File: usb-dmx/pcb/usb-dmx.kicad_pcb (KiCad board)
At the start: 2 copper layers, 25 x 35 mm, 21 parts, among them J1 USB_C_Receptacle_USB2.0_16P, J2 USB_A, SW1 PTS526_SM15_SMTR2_LFS, U1 IP4234CZ6, U2 ADP2108AUJ-3.3, U3 ESP32-S3-MINI-1U, U4 ST485E

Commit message: updating gerber files
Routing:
- net 15: track 22.0 -> 0.00 mm
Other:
- board text added: "TRANCE USB-DMX Rev: 1.1"
- board text removed: "TRANCE USB-DMX Rev: 1"
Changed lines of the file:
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@@
 			(psa4output no)
 			(plot_black_and_white yes)
-			(plotinvisibletext no)
 			(sketchpadsonfab no)
 			(plotpadnumbers no)
@@
 		)
 	)
-	(gr_text "TRANCE\nUSB-DMX\nRev: 1"
+	(gr_text "TRANCE\nUSB-DMX\nRev: 1.1"
 		(at 100 74 0)
 		(layer "B.SilkS")
@@
 		(layer "Cmts.User")
 		(pts
-			(xy 109.9 62) (xy 111.1 62)
+			(xy 109.6 62) (xy 111.4 62)
 		)
 		(height -5.5)
@@
 			(keep_text_aligned yes)
 		)
-		(gr_text "1.2"
+		(gr_text "1.8"
 			(at 110.5 55.35 0)
 			(layer "Cmts.User")
@@
 	)
 	(segment
-		(start 109.2 70.6)
-		(end 109.2 76.8)
-		(width 0.2)
-		(layer "F.Cu")
-		(net 8)
-	)
-	(segment
-		(start 103.997 74.551)
-		(end 106.449 74.551)
-		(width 0.2)
-		(layer "F.Cu")
-		(net 8)
-	)
-	(segment
-		(start 107.4 73.6)
-		(end 107.4 70.6)
-		(width 0.2)
-		(layer "F.Cu")
-		(net 8)
-	)
-	(segment
-		(start 107.4 70.6)
-		(end 107.8 70.2)
-		(width 0.2)
-		(layer "F.Cu")
-		(net 8)
-	)
-	(segment
-		(start 108.8 70.2)
-		(end 109.2 70.6)
-		(width 0.2)
-		(layer "F.Cu")
-		(net 8)
-	)
-	(segment
-		(start 99.4 79.148)
-		(end 103.997 74.551)
-		(width 0.2)
-		(layer "F.Cu")
-		(net 8)
-	)
-	(segment
-		(start 106.449 74.551)
-		(end 107.4 73.6)
-		(width 0.2)
-		(layer "F.Cu")
-		(net 8)
-	)
-	(segment
-		(start 107.8 70.2)
-		(end 108.8 70.2)
-		(width 0.2)
-		(layer "F.Cu")
-		(net 8)
-	)
-	(segment
-		(start 99.4 79.5)
-		(end 99.4 79.148)
-		(width 0.2)
-		(layer "F.Cu")
-		(net 8)
-	)
-	(segment
 		(start 100.4 76.6875)
 		(end 100.4125 76.7)
@@
 	)
 	(segment
+		(start 103.352 89.9)
+		(end 104 89.252)
+		(width 0.2)
+		(layer "F.Cu")
+		(net 15)
+	)
+	(segment
 		(start 107.7125 81.8)
 		(end 109.3375 81.8)
@@
 	)
 	(segment
-		(start 103.701 89.551)
-		(end 103.701 81.599)
+		(start 104 89.252)
+		(end 104 81.3)
 		(width 0.2)
 		(layer "F.Cu")
@@
 	)
 	(segment
-		(start 103.352 89.9)
-		(end 103.701 89.551)
+		(start 104 81.3)
+		(end 105.2 80.1)
 		(width 0.2)
 		(layer "F.Cu")
@@
 	)
 	(segment
-		(start 103.701 81.599)
-		(end 105.2 80.1)
-		(width 0.2)
-		(layer "F.Cu")
-		(net 15)
-	)
-	(segment
 		(start 109.5 81.8)
 		(end 111.2 80.1)
@@
 	)
 	(via
-		(at 104.9 86.9)
+		(at 105 86)
 		(size 0.6)
 		(drill 0.3)

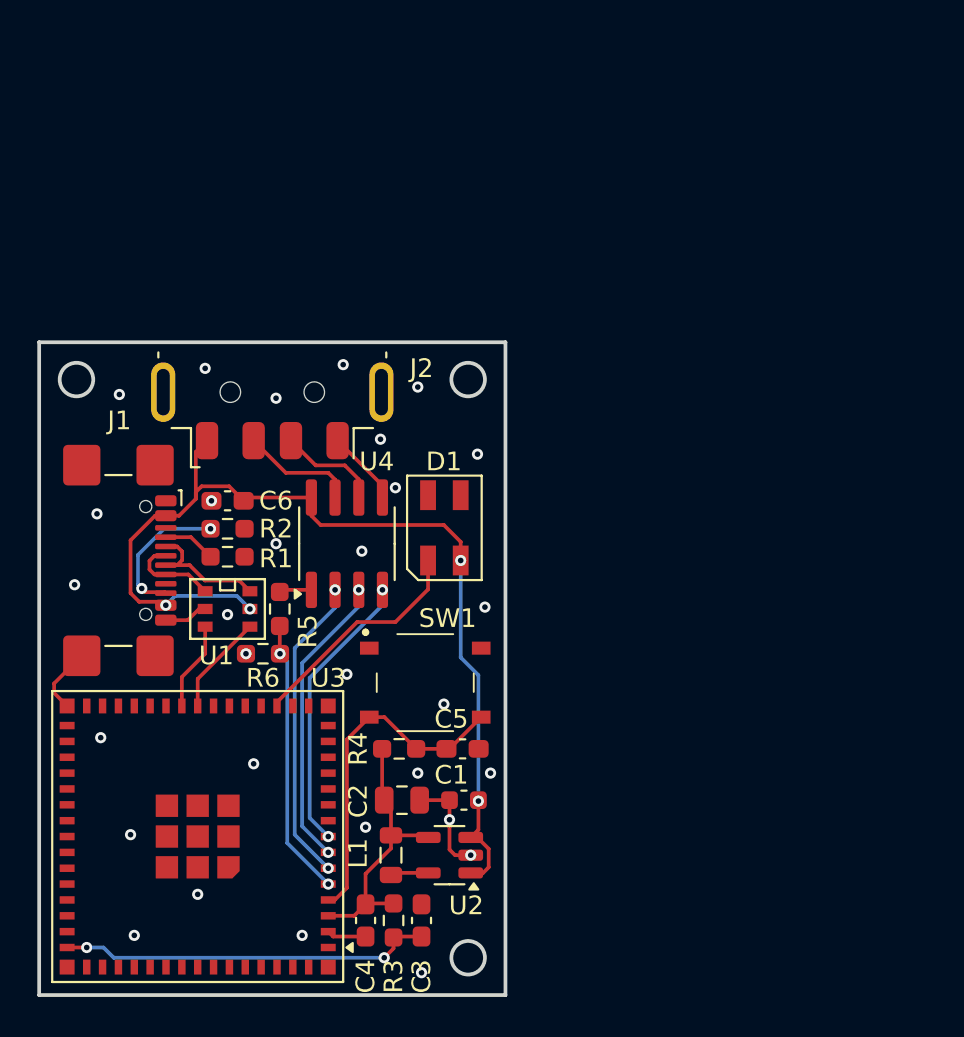
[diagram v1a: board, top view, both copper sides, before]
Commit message: adding larger capacitor to esp and exchanging parts
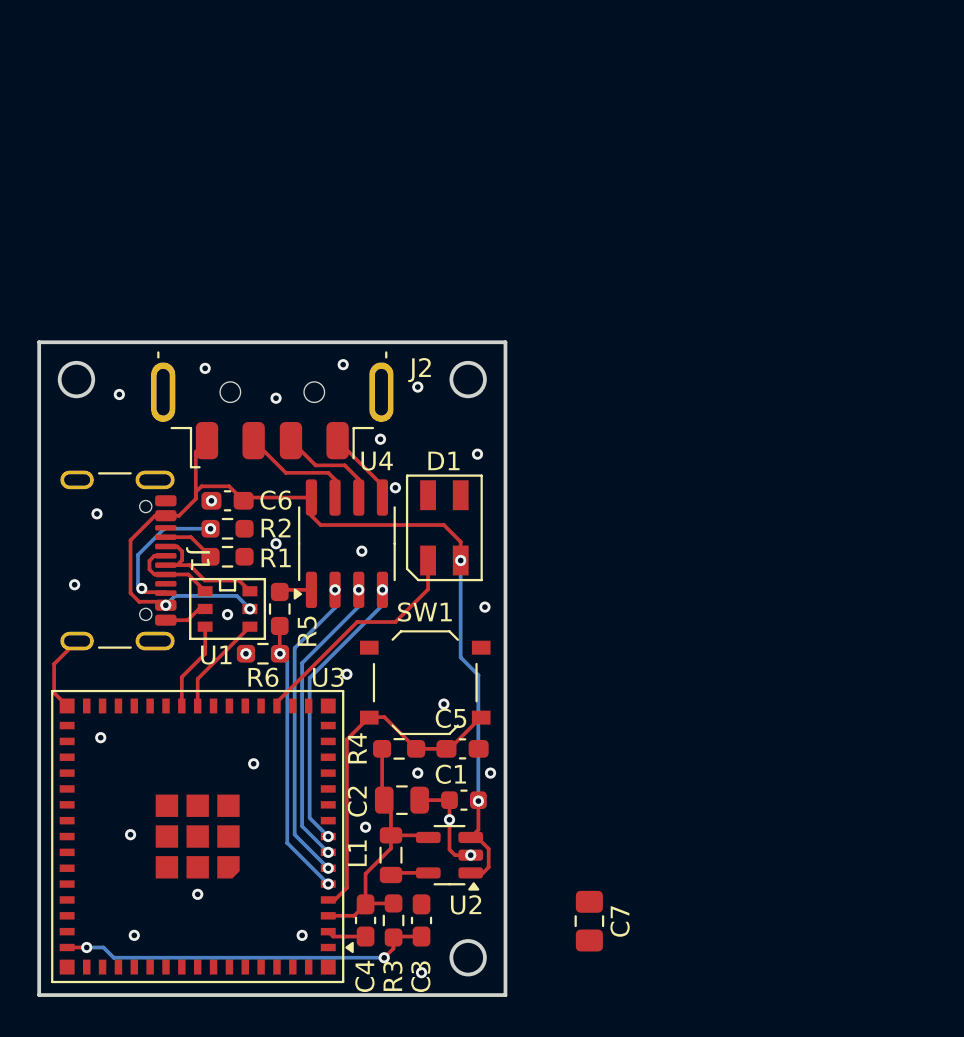
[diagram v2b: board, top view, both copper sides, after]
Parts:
- added C7: 47uF, Capacitor_SMD:C_0805_2012Metric_Pad1.18x1.45mm_HandSolder, F.Cu at (117.0, 91.0)
- J1: footprint Connector_USB:USB_C_Receptacle_GCT_USB4110 -> Connector_USB:USB_C_Receptacle_GCT_USB4105-xx-A_16P_TopMnt_Horizontal
- SW1: footprint footprints:PTS526SM15SMTR2LFS -> Button_Switch_SMD:SW_Push_1P1T_XKB_TS-1187A
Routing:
- net GND: track 17.6 -> 18.3 mm

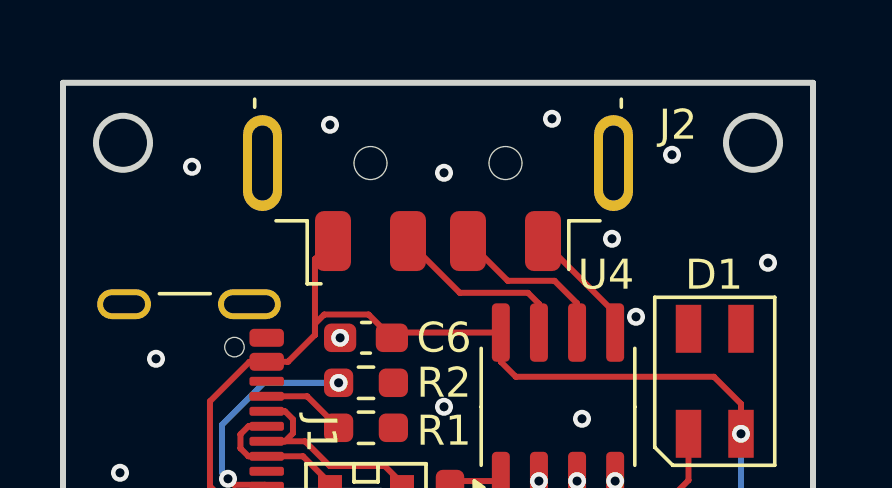
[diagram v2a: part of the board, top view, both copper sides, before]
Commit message: fingind aliexpress alternatives
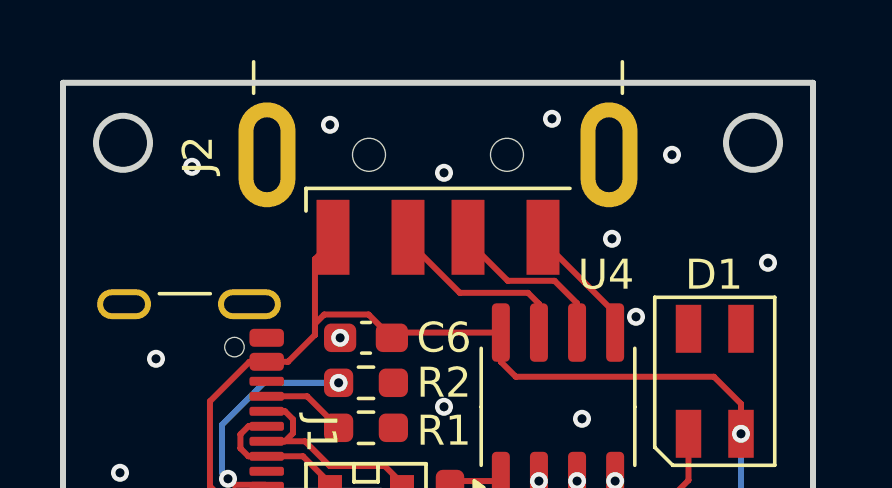
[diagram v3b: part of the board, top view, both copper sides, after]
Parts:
- J2: footprint Connector_USB:USB_A_Molex_48037-2200_Horizontal -> Connector_USB:USB_A_CNCTech_1001-011-01101_Horizontal
- moved J2 1.20 mm to (100.0, 55.5)

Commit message: creating pcb layout
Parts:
- removed L1: 1uH, Inductor_SMD:L_0805_2012Metric
- removed SW1: PTS526_SM15_SMTR2_LFS, Button_Switch_SMD:SW_Push_1P1T_XKB_TS-1187A
- removed U2: ADP2108AUJ-3.3, Package_TO_SOT_SMD:TSOT-23-5
- added SW2: SW_Push, Button_Switch_SMD:SW_Push_1P1T_XKB_TS-1187A, F.Cu at (94.1, 68.8)
- added U5: MAX485E, Package_SO:SOP-8_3.76x4.96mm_P1.27mm, F.Cu at (106.8, 55.5)
- C1: value 4.7uF -> 22uF; footprint Capacitor_SMD:C_0603_1608Metric -> Capacitor_SMD:C_0805_2012Metric
- C2: value 10uF -> 22uF
- C5: footprint Capacitor_SMD:C_0603_1608Metric_Pad1.08x0.95mm_HandSolder -> Capacitor_SMD:C_0603_1608Metric
- R4: footprint Resistor_SMD:R_0603_1608Metric_Pad0.98x0.95mm_HandSolder -> Resistor_SMD:R_0603_1608Metric
- U1: value IP4234CZ6 -> AMS1117-3.3; footprint footprints:IP4234CZ6_SOT-457-6 -> Package_TO_SOT_SMD:SOT-223-3_TabPin2
- U4: value ST485E -> USBLC6-2SC6; footprint Package_SO:SOIC-8_3.9x4.9mm_P1.27mm -> Package_TO_SOT_SMD:SOT-23-6
- moved C5 24.8 mm to (91.8, 65.2), turned to 180 degrees
- moved R6 20.7 mm to (100.2, 56.0), turned to 0 degrees
- moved R4 20.5 mm to (94.8, 65.2), turned to 180 degrees
- moved C2 17.6 mm to (99.2, 68.8), turned to 90 degrees
- moved R1 17.2 mm to (100.2, 54.5)
- moved R5 16.8 mm to (100.2, 57.5), turned to 0 degrees
- moved C6 15.7 mm to (100.2, 53.0), turned to 0 degrees
- moved J2 15.5 mm to (100.0, 40.0)
- moved J1 15.2 mm to (93.6, 56.8)
- moved C3 14.9 mm to (106.8, 76.2)
- moved C1 11.9 mm to (107.8, 72.9)
- moved C7 11.4 mm to (107.0, 85.5)
- moved R3 11.4 mm to (106.8, 79.7), turned to 90 degrees
- moved R2 11.3 mm to (100.2, 59.0)
- moved U1 9.51 mm to (104.8, 68.2)
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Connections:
- C1 pad 1: VCC_5V -> VCC_3.3V
- C2 pad 1: VCC_3.3V -> VCC_5V
- R5 pad 2: Net-(U4-RO) -> Net-(U5-RO)
- U1 pad 1: Net-(J1-D+-PadA6) -> GND
- U1 pad 2: GND -> VCC_3.3V
- U1 pad 3: D+ -> VCC_5V
- U4 pad 1: Net-(U4-RO) -> Net-(J1-D+-PadA6)
- U4 pad 2: 2 -> GND
- U4 pad 3: 3 -> Net-(J1-D--PadA7)
- U4 pad 4: 4 -> D-
- U4 pad 5: GND -> VCC_5V
- U4 pad 6: DMX+ -> D+
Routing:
- net GND: track 18.3 -> 45.0 mm, vias 30 -> 33
- net VCC_3.3V: track 14.9 -> 38.7 mm
- net 0: track 18.3 -> 40.3 mm, vias 0 -> 2
- net VCC_5V: track 54.2 -> 70.6 mm, vias 4 -> 2
- net 1: track 14.9 -> 29.6 mm
- net D+: track 4.77 -> 13.7 mm, vias 0 -> 2
- net 2: track 16.6 -> 24.9 mm
- net 3: track 15.9 -> 24.0 mm
- net 4: track 15.3 -> 23.2 mm
- net Net-(J1-D+-PadA6): track 4.92 -> 10.4 mm
- net D-: track 5.41 -> 10.0 mm, vias 0 -> 2
- net Net-(U5-RO): track 0.00 -> 3.80 mm
- net Net-(U3-EN): track 20.0 -> 23.5 mm
- net DMX-: track 6.19 -> 9.48 mm
- net DMX+: track 5.47 -> 8.34 mm
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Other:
- board size 25 x 35 mm -> 20 x 44 mm
- board text added: "${REFERENCE}"
- board text added: "TRANCE USB-DMX Rev: 1.2"
- board text removed: "TRANCE USB-DMX Rev: 1.1"

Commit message: updating documentation
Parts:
- moved C4 36.3 mm to (133.0, 58.8), turned to 0 degrees
- moved C7 35.9 mm to (132.8, 60.5), turned to 0 degrees
- moved U3 30.8 mm to (127.0, 69.5), turned to -90 degrees
- moved J2 30.3 mm to (87.2, 67.5), turned to 180 degrees
- moved R3 27.6 mm to (126.9, 60.6), turned to 180 degrees
- moved C5 23.3 mm to (112.5, 75.8), turned to -90 degrees
- moved C3 22.7 mm to (123.4, 60.6), turned to 180 degrees
- moved SW2 22.4 mm to (116.0, 73.4), turned to 90 degrees
- moved J1 20.1 mm to (104.1, 73.9), turned to 0 degrees
- moved R4 19.3 mm to (112.5, 72.8), turned to -90 degrees
- moved C1 18.1 mm to (120.2, 59.7), turned to -90 degrees
- moved C2 16.8 mm to (116.0, 68.2), turned to 180 degrees
- moved C6 14.2 mm to (100.2, 67.2), turned to 90 degrees
- moved R1 12.8 mm to (101.8, 67.2), turned to 90 degrees
- moved U1 11.9 mm to (115.4, 62.6), turned to 90 degrees
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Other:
- board size 20 x 44 mm -> 44 x 20 mm

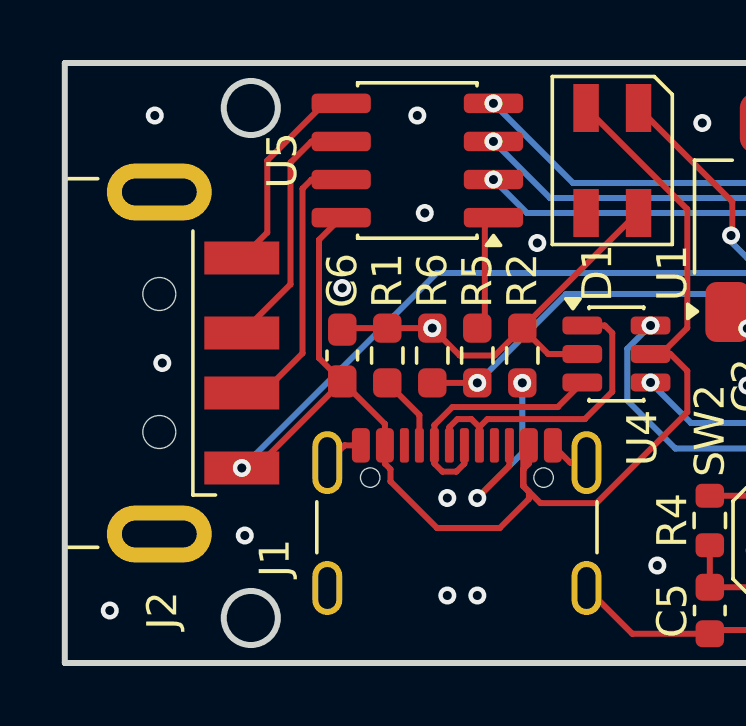
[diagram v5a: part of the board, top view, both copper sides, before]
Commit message: moving usb-a-plug, changing esp32-partnumber
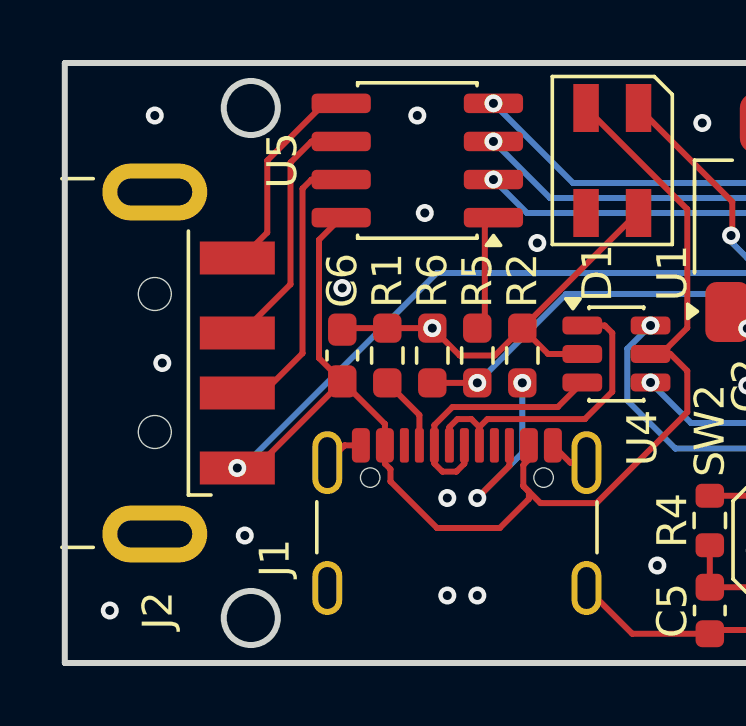
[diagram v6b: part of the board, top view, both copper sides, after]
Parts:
- moved J2 0.15 mm to (87.1, 67.5)
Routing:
- net VCC_5V: track 70.6 -> 69.4 mm
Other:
- board text added: "TRANCE USB-DMX Rev: 1.3"
- board text removed: "TRANCE USB-DMX Rev: 1.2"
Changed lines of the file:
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@@
 		(title "TRANCE USB-DMX")
 		(date "2025-12-23")
-		(rev "1.2")
+		(rev "1.3")
 		(company "Hafen Innovation")
 		(comment 1 "Author: Samuel Hafen")
@@
 			(drillshape 0)
 			(scaleselection 1)
-			(outputdirectory "gbr/")
+			(outputdirectory "gerber/")
 		)
 	)
@@
 	(footprint "Connector_USB:USB_A_CNCTech_1001-011-01101_Horizontal"
 		(layer "F.Cu")
-		(at 87.25 67.5 180)
+		(at 87.1 67.5 180)
 		(descr "USB type A Plug, Horizontal, http://cnctech.us/pdfs/1001-011-01101.pdf")
 		(tags "USB-A")
@@
 		)
 	)
-	(gr_text "TRANCE\nUSB-DMX\nRev: 1.2"
+	(gr_text "TRANCE\nUSB-DMX\nRev: 1.3"
 		(at 120 67.5 90)
 		(layer "B.SilkS")
@@
 	)
 	(segment
-		(start 106.47 70.245)
-		(end 106.284 70.431)
-		(width 0.2)
-		(layer "F.Cu")
-		(net 24)
-	)
-	(segment
 		(start 101.67 70.245)
 		(end 101.67 69.5325)
@@
 	)
 	(segment
-		(start 97.3625 71)
-		(end 100.25 68.1125)
+		(start 106.47 70.245)
+		(end 106.47 70.714)
 		(width 0.2)
 		(layer "F.Cu")
@@
 	)
 	(segment
-		(start 111.75 62.375)
-		(end 108.375 59)
+		(start 96.75 71)
+		(end 97.3625 71)
 		(width 0.2)
 		(layer "F.Cu")
@@
 	)
 	(segment
-		(start 96.9 71)
-		(end 97.3625 71)
+		(start 111.75 62.375)
+		(end 108.375 59)
 		(width 0.2)
 		(layer "F.Cu")
@@
 	)
 	(segment
-		(start 106.47 70.853992)
-		(end 106.284 71.039992)
+		(start 97.3625 71)
+		(end 100.25 68.1125)
 		(width 0.2)
 		(layer "F.Cu")
@@
 	)
 	(segment
-		(start 106.284 70.431)
+		(start 106.47 70.714)
+		(end 106.284 70.9)
+		(width 0.2)
+		(layer "F.Cu")
+		(net 24)
+	)
+	(segment
+		(start 106.284 70.9)
 		(end 106.284 71.600008)
 		(width 0.2)
@@
 	)
 	(segment
-		(start 106.47 70.245)
-		(end 106.47 70.853992)
-		(width 0.2)
-		(layer "F.Cu")
-		(net 24)
-	)
-	(segment
 		(start 116.95 68.25)
 		(end 116.95 66.55)
@@
 	)
 	(segment
-		(start 106.284 71.039992)
-		(end 106.284 71.600008)
-		(width 0.2)
-		(layer "F.Cu")
-		(net 24)
-	)
-	(segment
 		(start 110.525 67.2)
 		(end 110.879468 67.2)
@@
 	)
 	(via
-		(at 96.9 71)
+		(at 96.75 71)
 		(size 0.6)
 		(drill 0.3)
@@
 	)
 	(segment
-		(start 96.9 71)
-		(end 103.4 64.5)
+		(start 116.4 64.5)
+		(end 117.7 65.8)
 		(width 0.2)
 		(layer "B.Cu")
@@
 	)
 	(segment
-		(start 116.4 64.5)
-		(end 117.7 65.8)
+		(start 103.4 64.5)
+		(end 116.4 64.5)
 		(width 0.2)
 		(layer "B.Cu")
@@
 	)
 	(segment
-		(start 103.4 64.5)
-		(end 116.4 64.5)
+		(start 96.75 71)
+		(end 96.9 71)
+		(width 0.2)
+		(layer "B.Cu")
+		(net 24)
+	)
+	(segment
+		(start 96.9 71)
+		(end 103.4 64.5)
 		(width 0.2)
 		(layer "B.Cu")
